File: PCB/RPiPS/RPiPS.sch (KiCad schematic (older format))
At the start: 17 parts, among them IC1 ATTINY25-P, K1 RELAI-1RT, P1 PowerIn, P2 CONN_1, P3 PiPower, Q1 NPN, SW1 SW_PUSH

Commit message: Typon
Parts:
- R2: value R -> 30K
- R3, R5: value R -> 1K
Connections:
- net GND: now also D4.2 (K); no longer R4.2
- net at IC1.2 (PB3(XTAL1/CLKI/OC1B/ADC3/PCINT3)): now also R4.1; no longer D4.1 (A)
- new net: D4.1 (A), R4.2
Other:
- moved on the sheet: D4, R4
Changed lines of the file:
@@
 LIBS:valves
 LIBS:local
+LIBS:RPiPS-cache
 EELAYER 24 0
 EELAYER END
@@
 P 6950 3900
 F 0 "R3" V 7030 3900 40  0000 C CNN
-F 1 "R" V 6957 3901 40  0000 C CNN
+F 1 "1K" V 6957 3901 40  0000 C CNN
 F 2 "" V 6880 3900 30  0000 C CNN
 F 3 "" H 6950 3900 30  0000 C CNN
@@
 L LED D4
 U 1 1 52C97AD6
-P 7150 4750
-F 0 "D4" H 7150 4850 50  0000 C CNN
-F 1 "LED" H 7150 4650 50  0000 C CNN
-F 2 "" H 7150 4750 60  0000 C CNN
-F 3 "" H 7150 4750 60  0000 C CNN
-	1    7150 4750
+P 7150 5250
+F 0 "D4" H 7150 5350 50  0000 C CNN
+F 1 "LED" H 7150 5150 50  0000 C CNN
+F 2 "" H 7150 5250 60  0000 C CNN
+F 3 "" H 7150 5250 60  0000 C CNN
+	1    7150 5250
 	0    1    1    0
 $EndComp
@@
 L R R4
 U 1 1 52C97AEA
-P 7150 5200
-F 0 "R4" V 7230 5200 40  0000 C CNN
-F 1 "R" V 7157 5201 40  0000 C CNN
-F 2 "" V 7080 5200 30  0000 C CNN
-F 3 "" H 7150 5200 30  0000 C CNN
-	1    7150 5200
+P 7150 4800
+F 0 "R4" V 7230 4800 40  0000 C CNN
+F 1 "R" V 7157 4801 40  0000 C CNN
+F 2 "" V 7080 4800 30  0000 C CNN
+F 3 "" H 7150 4800 30  0000 C CNN
+	1    7150 4800
 	1    0    0    -1
 $EndComp
@@
 P 6650 5000
 F 0 "R2" V 6730 5000 40  0000 C CNN
-F 1 "R" V 6657 5001 40  0000 C CNN
+F 1 "30K" V 6657 5001 40  0000 C CNN
 F 2 "" V 6580 5000 30  0000 C CNN
 F 3 "" H 6650 5000 30  0000 C CNN
@@
 P 7900 4500
 F 0 "R5" V 7980 4500 40  0000 C CNN
-F 1 "R" V 7907 4501 40  0000 C CNN
+F 1 "1K" V 7907 4501 40  0000 C CNN
 F 2 "" V 7830 4500 30  0000 C CNN
 F 3 "" H 7900 4500 30  0000 C CNN

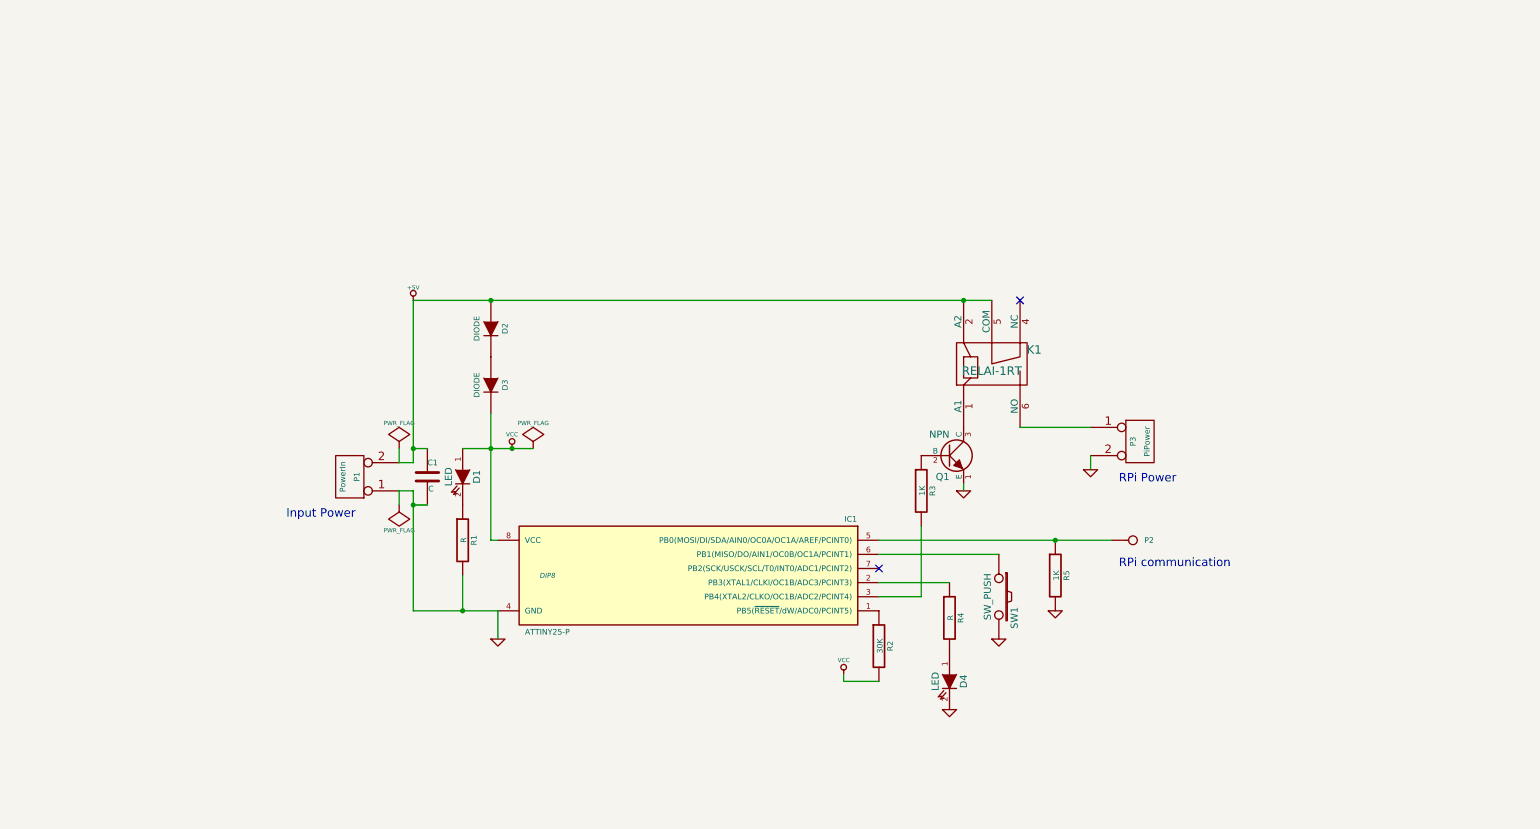
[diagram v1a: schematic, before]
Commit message: Move to RPi Expansion board template
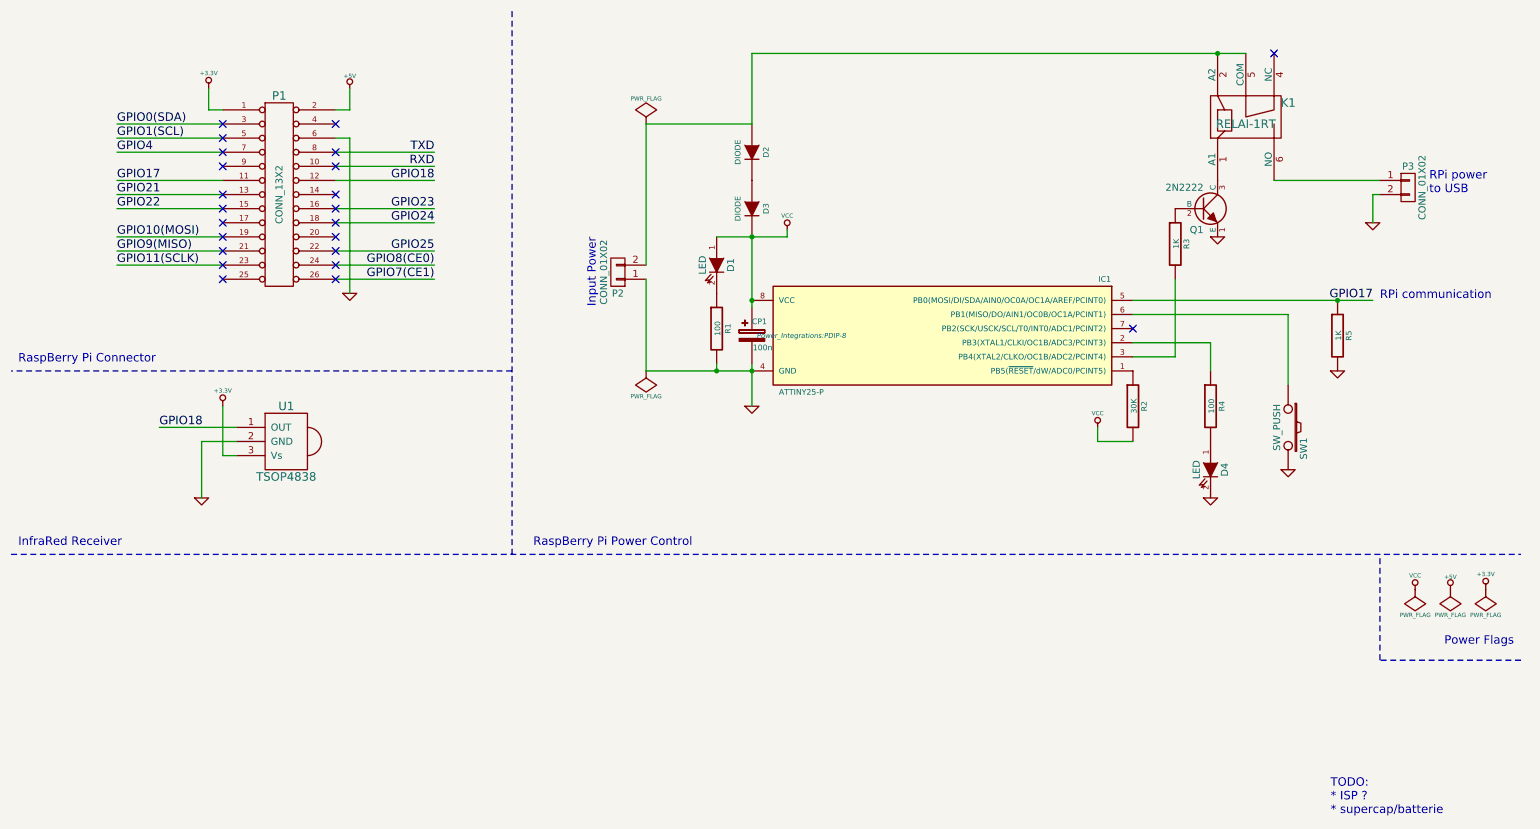
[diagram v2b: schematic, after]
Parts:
- removed C1: C, symbol C
- removed P1: PowerIn, symbol CONN_2
- removed P2: CONN_1, symbol CONN_1
- removed P3: PiPower, symbol CONN_2
- added CP1: 100n, Capacitors_Elko_ThroughHole:Elko_vert_DM5_RM2-5, symbol CP2
- added P1: CONN_13X2, Pin_Arrays:pin_array_2x13, symbol CONN_13X2
- added P2, P3: CONN_01X02, Connect:bornier2, symbol CONN_01X02
- added U1: TSOP4838, Housings_TO-92:TO-92-Bipolar-inline-wide-ECB, symbol TSOP4838
- D1, D4: footprint (none) -> LEDs:LED-5MM
- D2, D3: footprint (none) -> Diodes_ThroughHole:Diode_DO-35_SOD27_Horizontal_RM10
- IC1: footprint DIP8 -> Power_Integrations:PDIP-8
- K1: footprint (none) -> relay:Relay V23040
- Q1: value NPN -> 2N2222; footprint (none) -> Housings_TO-92:TO-92-Bipolar-inline-wide-CBE
- R1, R4: value R -> 100; footprint (none) -> Resistors_ThroughHole:Resistor_Horizontal_RM10mm
- R2, R3, R5: footprint (none) -> Resistors_ThroughHole:Resistor_Horizontal_RM10mm
- SW1: footprint (none) -> Discret:SW_PUSH
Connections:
- net +5V: now also P1.2 (P2); no longer D2.1 (A), K1.2 (A2), K1.5 (COM)
- net GND: now also CP1.2, P1.6 (P6), P2.1 (P1), P3.2 (P2), U1.2 (GND)
- net VCC: now also CP1.1
- net GPIO17: now reaches IC1.5 (PB0(MOSI/DI/SDA/AIN0/OC0A/OC1A/AREF/PCINT0)), R5.1
- net GPIO17: now also P1.11 (P11)
- net at K1.6 (NO): now also P3.1 (P1)
- new net: D2.1 (A), K1.2 (A2), K1.5 (COM), P2.2 (P2)
- new net +3.3V: P1.1 (P1), U1.3 (Vs)
- new net GPIO0(SDA): P1.3 (P3)
- new net GPIO1(SCL): P1.5 (P5)
- new net GPIO10(MOSI): P1.19 (P19)
- new net GPIO11(SCLK): P1.23 (P23)
- new net GPIO18: P1.12 (P12), U1.1 (OUT)
- new net GPIO21: P1.13 (P13)
- new net GPIO22: P1.15 (P15)
- new net GPIO23: P1.16 (P16)
- new net GPIO24: P1.18 (P18)
- new net GPIO25: P1.22 (P22)
- new net GPIO4: P1.7 (P7)
- new net GPIO7(CE1): P1.26 (P22)
- new net GPIO8(CE0): P1.24 (P20)
- new net GPIO9(MISO): P1.21 (P21)
- new net RXD: P1.10 (P10)
- new net TXD: P1.8 (P8)
- no-connect marks 2 -> 23
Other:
- note added: "InfraRed Receiver"
- note added: "Power Flags"
- note added: "RPi power\nto USB"
- note added: "RaspBerry Pi Connector"
- note added: "RaspBerry Pi Power Control"
- note added: "TODO:\n* ISP ?\n* supercap/batterie"
- note removed: "RPi Power"

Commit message: add IR receiver pcb routing fabrication files
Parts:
- removed Q1: 2N2222, Housings_TO-92:TO-92-Bipolar-inline-wide-CBE, symbol NPN
- added Q1: PN2222A, Discret:TO92-123, symbol PN2222A
- U1: footprint Housings_TO-92:TO-92-Bipolar-inline-wide-ECB -> IR:TSOP4838
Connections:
- net +5V: now also P1.4 (P4)
- net GND: now also P1.14 (P14), P1.20 (P20), P1.25 (P24), P1.9 (P9), Q1.2 (E)
- net at R3.1: now also Q1.1 (B)
- net at K1.1 (A1): now also Q1.3 (C)
- no-connect marks 23 -> 18
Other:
- note added: "boot ok"
- note added: "power on"
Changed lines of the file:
@@
 $EndComp
 Wire Wire Line
-	2900 1050 2900 1200
+	2900 1050 2900 1300
 Wire Wire Line
 	2900 1200 2800 1200
-NoConn ~ 2800 1300
 Wire Wire Line
 	2000 1300 1250 1300
@@
 Text Label 1250 1500 0    60   ~ 0
 GPIO4
-NoConn ~ 2000 1600
 Wire Wire Line
 	2000 1700 1250 1700
@@
 Text Label 1250 2300 0    60   ~ 0
 GPIO11(SCLK)
-NoConn ~ 2000 2400
 $Comp
 L GND #PWR03
@@
 Text Label 3500 1700 2    60   ~ 0
 GPIO18
-NoConn ~ 2800 1800
 Wire Wire Line
 	2800 1900 3500 1900
@@
 Text Label 3500 2000 2    60   ~ 0
 GPIO24
-NoConn ~ 2800 2100
 Wire Wire Line
 	2800 2200 3500 2200
@@
 Wire Wire Line
 	5500 2100 6000 2100
-$Comp
-L NPN Q1
-U 1 1 5426B8E9
-P 8950 1900
-F 0 "Q1" H 8950 1750 50  0000 R CNN
-F 1 "2N2222" H 8950 2050 50  0000 R CNN
-F 2 "Housings_TO-92:TO-92-Bipolar-inline-wide-CBE" H 8950 1900 60  0001 C CNN
-F 3 "" H 8950 1900 60  0000 C CNN
-	1    8950 1900
-	1    0    0    -1
-$EndComp
 $Comp
 L R R3
@@
 F 0 "U1" H 2450 3800 60  0000 C CNN
 F 1 "TSOP4838" H 2450 3300 60  0000 C CNN
-F 2 "Housings_TO-92:TO-92-Bipolar-inline-wide-ECB" H 2300 3550 60  0001 C CNN
+F 2 "IR:TSOP4838" H 2300 3550 60  0001 C CNN
 F 3 "" H 2300 3550 60  0000 C CNN
 	1    2300 3550
@@
 Wire Notes Line
 	10200 5100 10200 4350
+$Comp
+L PN2222A Q1
+U 1 1 5427E170
+P 8950 1900
+F 0 "Q1" H 8950 1752 40  0000 R CNN
+F 1 "PN2222A" H 8950 2050 40  0000 R CNN
+F 2 "Discret:TO92-123" H 8850 2002 29  0000 C CNN
+F 3 "" H 8950 1900 60  0000 C CNN
+	1    8950 1900
+	1    0    0    -1
+$EndComp
+Wire Wire Line
+	2900 1300 2800 1300
+Connection ~ 2900 1200
+Wire Wire Line
+	2000 1600 1950 1600
+Wire Wire Line
+	1950 1600 1950 2500
+$Comp
+L GND #PWR022
+U 1 1 54280058
+P 1950 2500
+F 0 "#PWR022" H 1950 2500 30  0001 C CNN
+F 1 "GND" H 1950 2430 30  0001 C CNN
+F 2 "" H 1950 2500 60  0001 C CNN
+F 3 "" H 1950 2500 60  0001 C CNN
+	1    1950 2500
+	1    0    0    -1
+$EndComp
+Wire Wire Line
+	2800 1800 2900 1800
+Connection ~ 2900 1800
+Wire Wire Line
+	2800 2100 2900 2100
+Connection ~ 2900 2100
+Wire Wire Line
+	2000 2400 1950 2400
+Connection ~ 1950 2400
+Text Notes 5350 2450 1    60   ~ 0
+power on
+Text Notes 8850 3900 1    60   ~ 0
+boot ok
 $EndSCHEMATC

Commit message: OSHW logo relay footprint
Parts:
- K1: footprint relay:Relay V23040 -> relay:Relay_V23040
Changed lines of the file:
@@
 F 0 "K1" H 9550 1150 60  0000 C CNN
 F 1 "RELAI-1RT" H 9250 1300 60  0000 C CNN
-F 2 "relay:Relay V23040" H 9250 1250 60  0001 C CNN
+F 2 "relay:Relay_V23040" H 9250 1250 60  0001 C CNN
 F 3 "" H 9250 1250 60  0000 C CNN
 	1    9250 1250

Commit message: remove gnd plane over Pi connectors reverse P2 (1 is +) minor Silk adjustment
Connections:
- net GND: now also P2.2 (P2); no longer P2.1 (P1)
- net at D2.1 (A), K1.2 (A2), K1.5 (COM): now also P2.1 (P1); no longer P2.2 (P2)
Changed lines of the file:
@@
 F 3 "" H 4800 2350 60  0000 C CNN
 	1    4800 2350
-	-1   0    0    1
+	-1   0    0    -1
 $EndComp
 Wire Wire Line
